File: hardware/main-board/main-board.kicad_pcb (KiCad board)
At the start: 2 copper layers, 180 x 55 mm, 96 parts, among them J1 BARREL_JACK, J2 CONN_01X10, J3 CONN_01X10, J4 USB_OTG, J5 CONN_02X05, J6 SMA, Q1 DDTD113ZC, Q2 DDTD113ZC, Q3 DDTD113ZC, Q4 DDTD113ZC, Q5 DDTD113ZC, Q6 FDB14N30TM, Q7 DDTD113ZC, Q8 DDTD113ZC, Q9 DDTD113ZC, SW1 SW_Push, SW2 SW_Push, SW3 SW_Push, SW4 SW_Push, U1 LD1117S33TR, U2 MAX1771, U3 STM32F302C, U4 FGPMMOPA6H, Y1 8MHz, Y2 32.768kHz

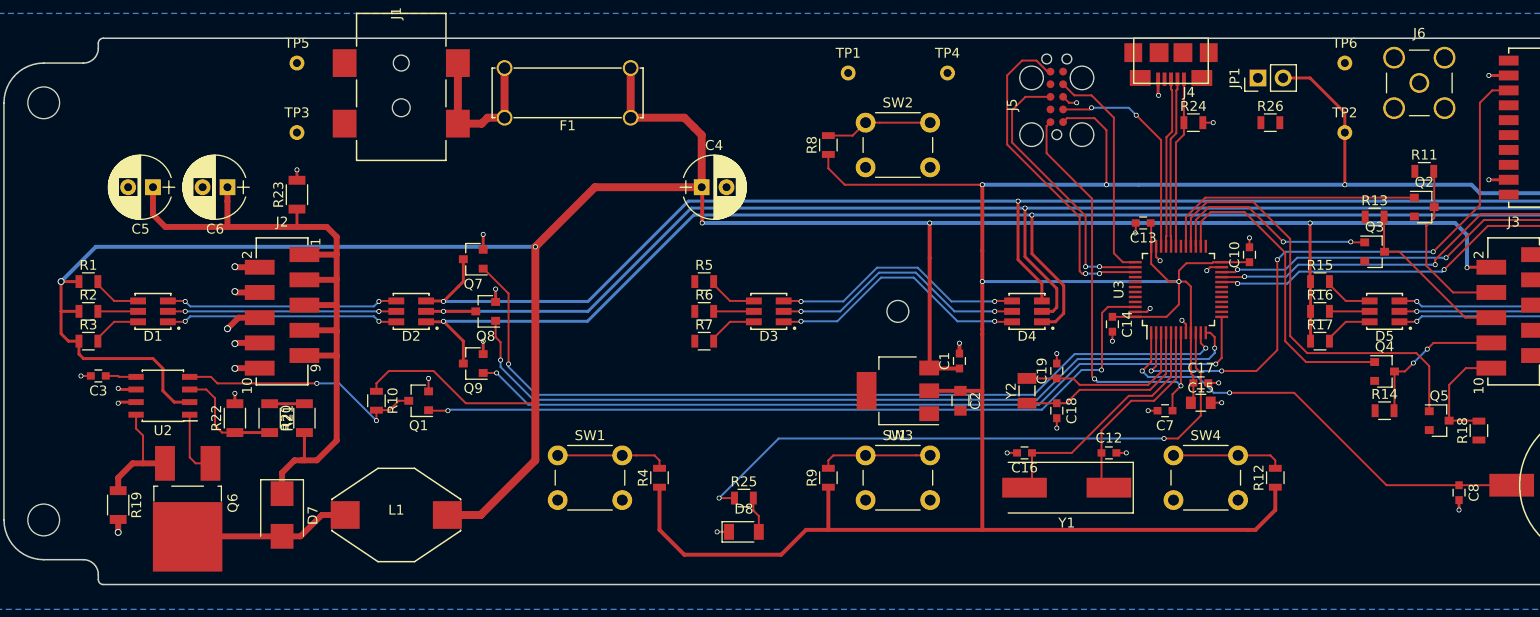
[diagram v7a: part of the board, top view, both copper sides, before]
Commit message: Working on main board layout
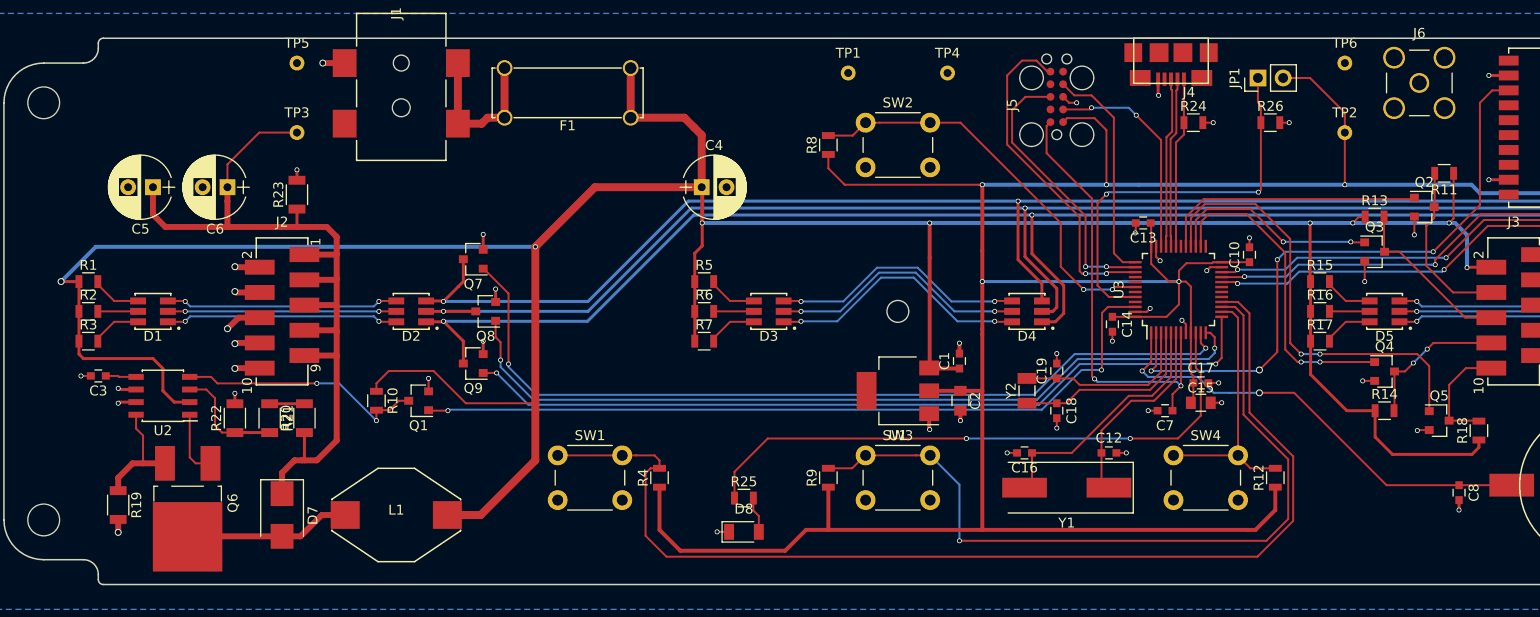
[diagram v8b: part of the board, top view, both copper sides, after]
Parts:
- moved R11 2.01 mm to (205.0, 76.1), turned to 180 degrees
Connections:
- U3 pad 14: /PB1 -> /PB3
- U3 pad 16: /PB3 -> /PB1
- U3 pad 17: /PB4 -> Net-(U3-Pad17)
- U3 pad 42: Net-(U3-Pad42) -> /PB4
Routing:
- net /PB1: track 11.3 -> 112.7 mm
- net /PB2: track 11.3 -> 79.5 mm, vias 0 -> 1
- net +12V: track 281.1 -> 323.1 mm, vias 6 -> 8
- net /BOOT0: track 0.00 -> 41.0 mm, vias 0 -> 2
- net /PB4: track 10.8 -> 41.1 mm, vias 0 -> 2
- net /PB3: track 11.3 -> 26.6 mm
- net GND: track 78.1 -> 90.2 mm, vias 48 -> 56
- net HT: track 76.6 -> 87.3 mm
- net /DGB_LED: track 62.0 -> 60.5 mm
- net /DISP_CLK: track 31.8 -> 32.2 mm, vias 0 -> 2
- net /DISP_DATA: track 44.6 -> 44.9 mm, vias 0 -> 2
